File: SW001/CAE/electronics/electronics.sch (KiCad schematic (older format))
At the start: 2 parts, among them J1 Conn_02x30_Counter_Clockwise

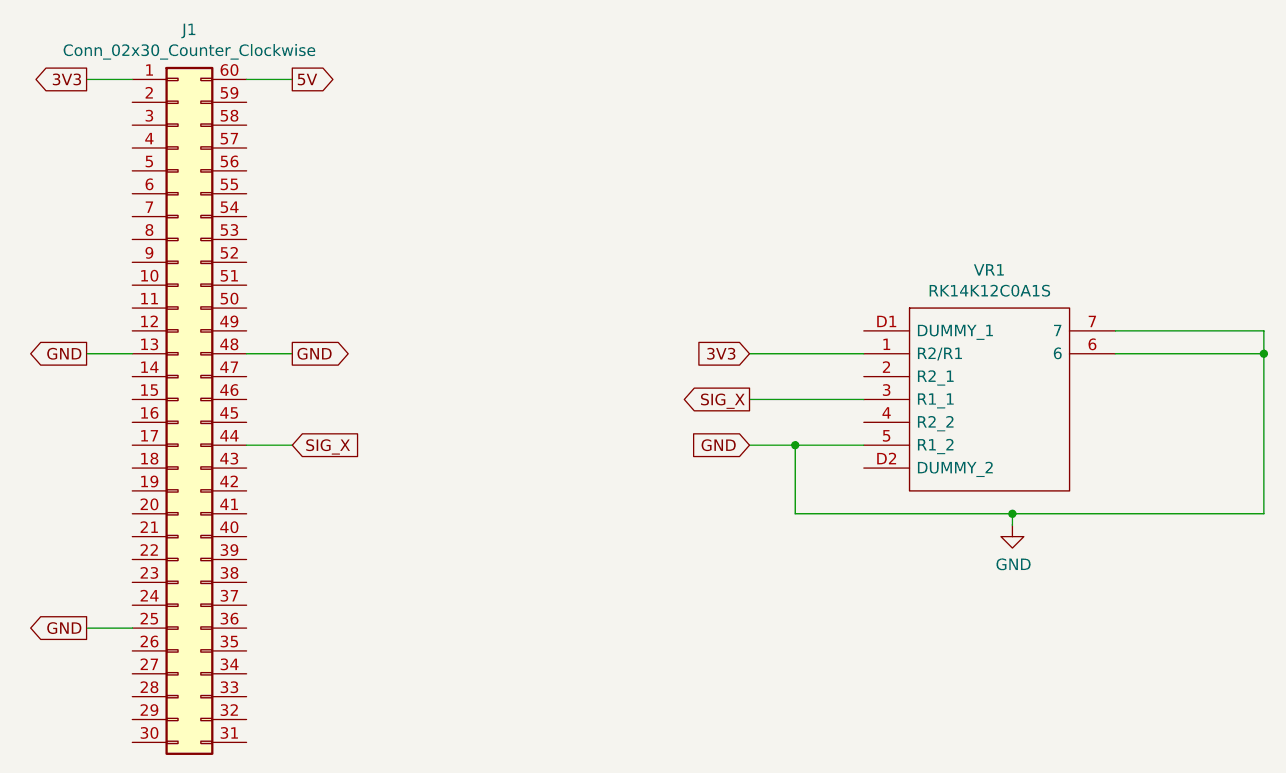
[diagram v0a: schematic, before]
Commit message: Planet gear updated Signed-off-by: Reisen-Wandern-Tauchen <webmaster@reisen-wandern-tauchen.at>
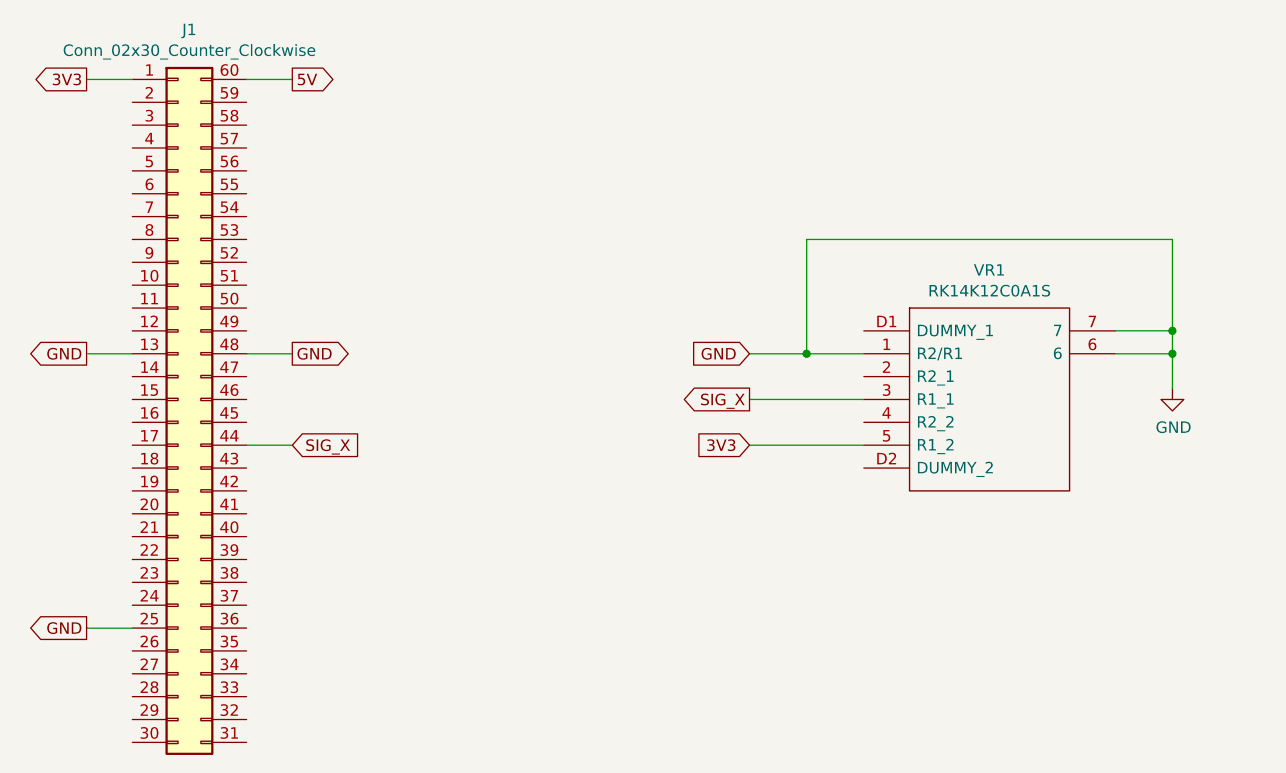
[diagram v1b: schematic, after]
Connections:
- net 3V3: now also VR1.5 (R1_2); no longer VR1.1 (R2/R1)
- net GND: now also VR1.1 (R2/R1); no longer VR1.5 (R1_2)
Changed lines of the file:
@@
 $EndComp
 Wire Wire Line
-	5950 2850 5450 2850
+	5950 2850 5700 2850
 Wire Wire Line
 	5950 3050 5450 3050
 Wire Wire Line
-	5950 3250 5650 3250
+	7050 2750 7300 2750
 Wire Wire Line
-	7050 2750 7700 2750
+	7300 2750 7300 2850
 Wire Wire Line
-	7700 2750 7700 2850
+	7050 2850 7300 2850
+Connection ~ 7300 2850
 Wire Wire Line
-	7050 2850 7700 2850
-Connection ~ 7700 2850
-Wire Wire Line
-	7700 2850 7700 3550
-Wire Wire Line
-	5650 3250 5650 3550
-Connection ~ 5650 3250
-Wire Wire Line
-	5650 3250 5450 3250
-Wire Wire Line
-	5650 3550 6600 3550
+	7300 2850 7300 3000
 $Comp
-L power:GND #PWR?
+L power:GND #PWR0101
 U 1 1 5EE2582F
-P 6600 3600
-F 0 "#PWR?" H 6600 3350 50  0001 C CNN
-F 1 "GND" H 6605 3427 50  0000 C CNN
-F 2 "" H 6600 3600 50  0001 C CNN
-F 3 "" H 6600 3600 50  0001 C CNN
-	1    6600 3600
+P 7300 3000
+F 0 "#PWR0101" H 7300 2750 50  0001 C CNN
+F 1 "GND" H 7305 2827 50  0000 C CNN
+F 2 "" H 7300 3000 50  0001 C CNN
+F 3 "" H 7300 3000 50  0001 C CNN
+	1    7300 3000
 	1    0    0    -1
 $EndComp
-Wire Wire Line
-	6600 3600 6600 3550
-Connection ~ 6600 3550
-Wire Wire Line
-	6600 3550 7700 3550
 Text GLabel 2550 1650 0    50   Output ~ 0
 3V3
@@
 Wire Wire Line
 	3450 1650 3250 1650
+Text GLabel 5450 3250 0    50   Input ~ 0
+3V3
 Text GLabel 5450 2850 0    50   Input ~ 0
-3V3
-Text GLabel 5450 3250 0    50   Input ~ 0
 GND
 Text GLabel 5450 3050 0    50   Output ~ 0
@@
 	1    0    0    -1
 $EndComp
+Wire Wire Line
+	5450 3250 5950 3250
+Wire Wire Line
+	7300 2750 7300 2350
+Wire Wire Line
+	7300 2350 5700 2350
+Wire Wire Line
+	5700 2350 5700 2850
+Connection ~ 7300 2750
+Connection ~ 5700 2850
+Wire Wire Line
+	5700 2850 5450 2850
 $EndSCHEMATC
